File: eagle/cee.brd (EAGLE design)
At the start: 50 x 80 mm, 63 parts, among them IC1 IC1, J1 SOLDERJUMPERNC2

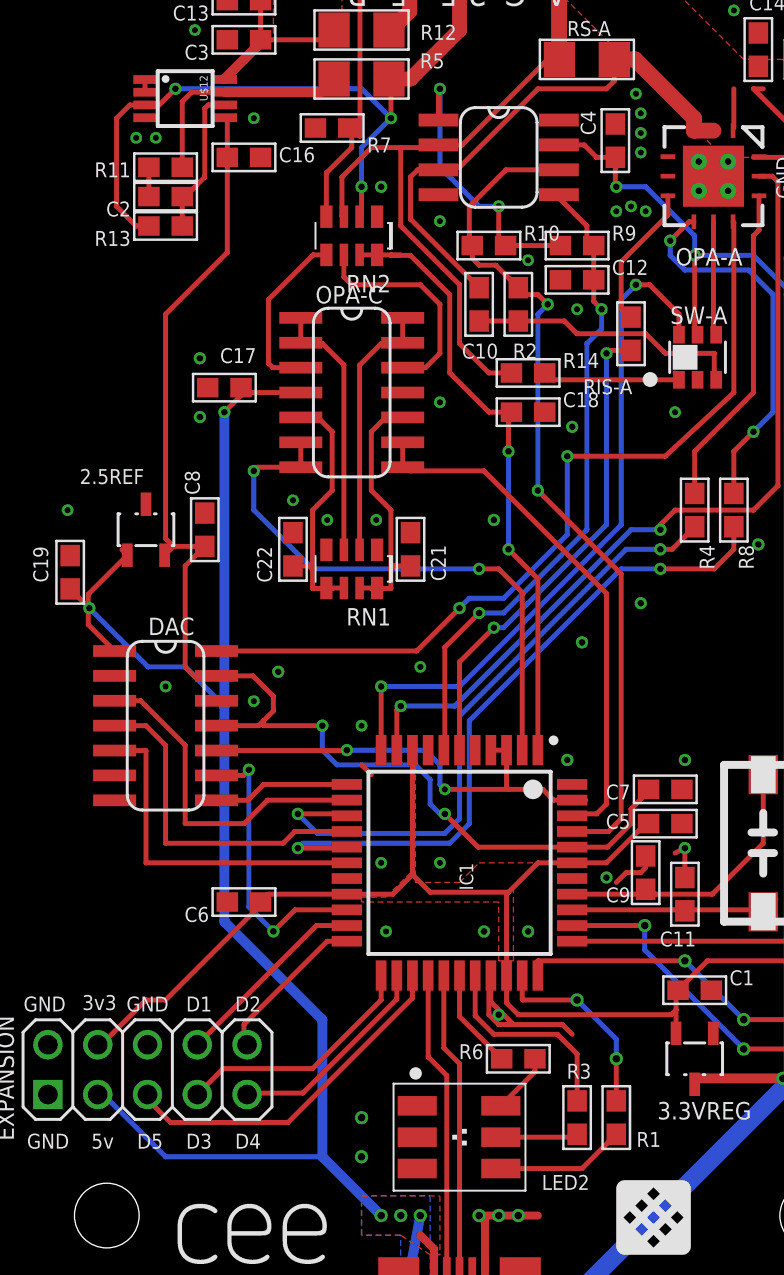
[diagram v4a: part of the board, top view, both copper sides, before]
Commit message: Connect CSA EN pin
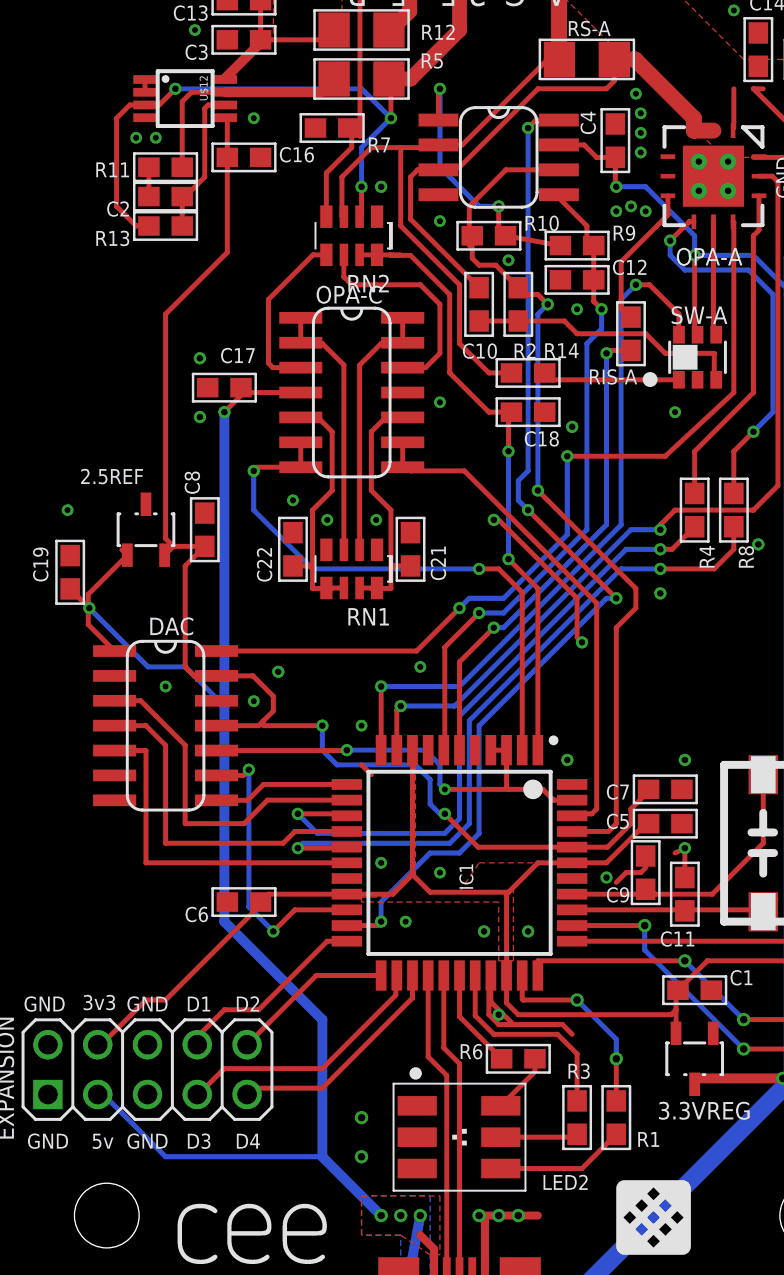
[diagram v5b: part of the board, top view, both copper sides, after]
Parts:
- moved R10 0.50 mm to (26.5, 57.0)
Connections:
- removed net EN-CSA: U$13.8
- removed net EXP5: EXPANSION.5, IC1.25
- new net CSA-EN: IC1.21, U$13.8
- net EXP1: now also IC1.22; no longer IC1.21
- net EXP2: now also IC1.23; no longer IC1.22
- net EXP3: now also IC1.24; no longer IC1.23
- net EXP4: now also IC1.25; no longer IC1.24
- net GND: now also EXPANSION.5
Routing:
- net CSA-EN: track 0.00 -> 52.5 mm, vias 0 -> 4
- net EXP5: track 18.1 -> 0.00 mm
- net GND: track 20.2 -> 27.9 mm
- net VS-A: track 44.0 -> 45.4 mm
- net ADC-A: track 27.2 -> 26.0 mm
- net EXP4: track 10.9 -> 11.7 mm
- net VOUT-B: track 23.3 -> 22.6 mm
- net EXP3: track 12.6 -> 13.3 mm
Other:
- board text removed: "D5"

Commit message: Rename VOUT-B -> ADCREF
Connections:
- net VOUT-B renamed ADCREF
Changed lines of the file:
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@@
 <wire x1="25.5" y1="38.5" x2="25" y2="38" width="0.254" layer="16"/>
 </signal>
-<signal name="VOUT-B">
+<signal name="ADCREF">
 <contactref element="DAC" pad="10"/>
 <contactref element="IC1" pad="4"/>

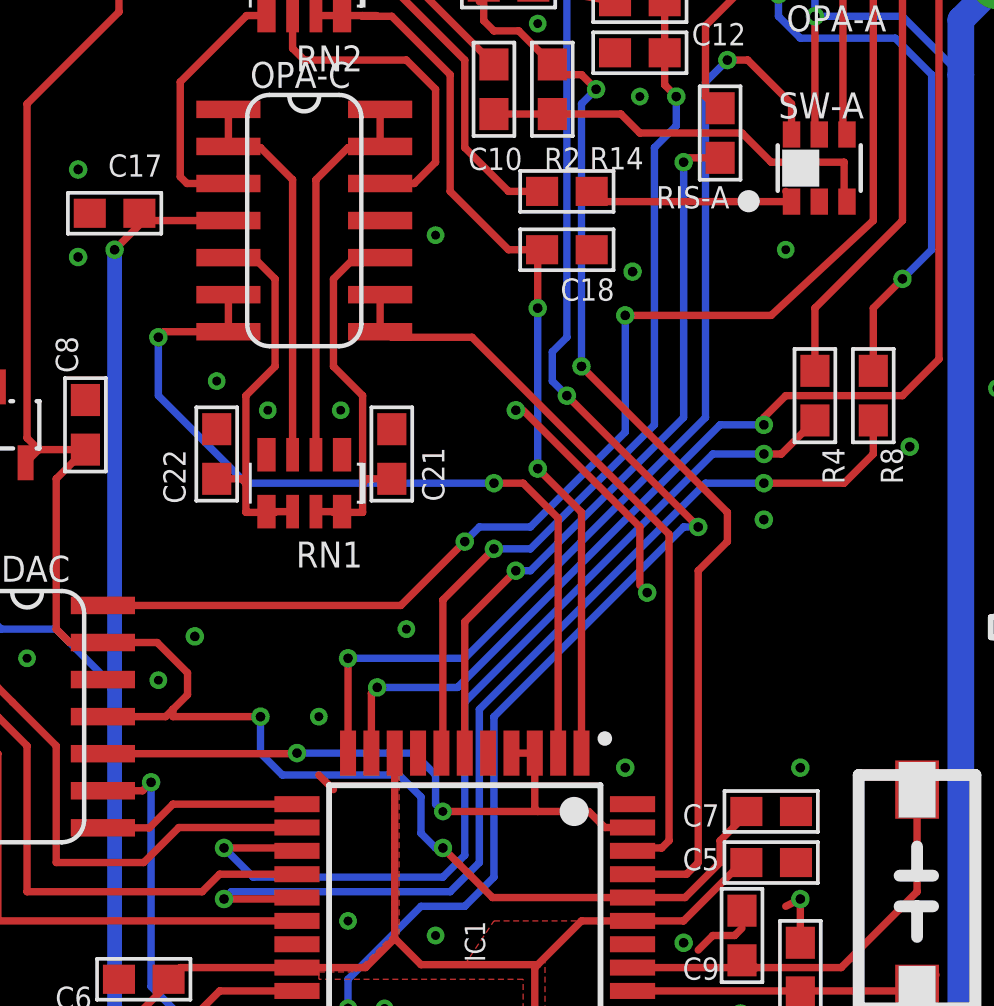
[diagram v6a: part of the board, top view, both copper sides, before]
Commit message: Clean up schematic
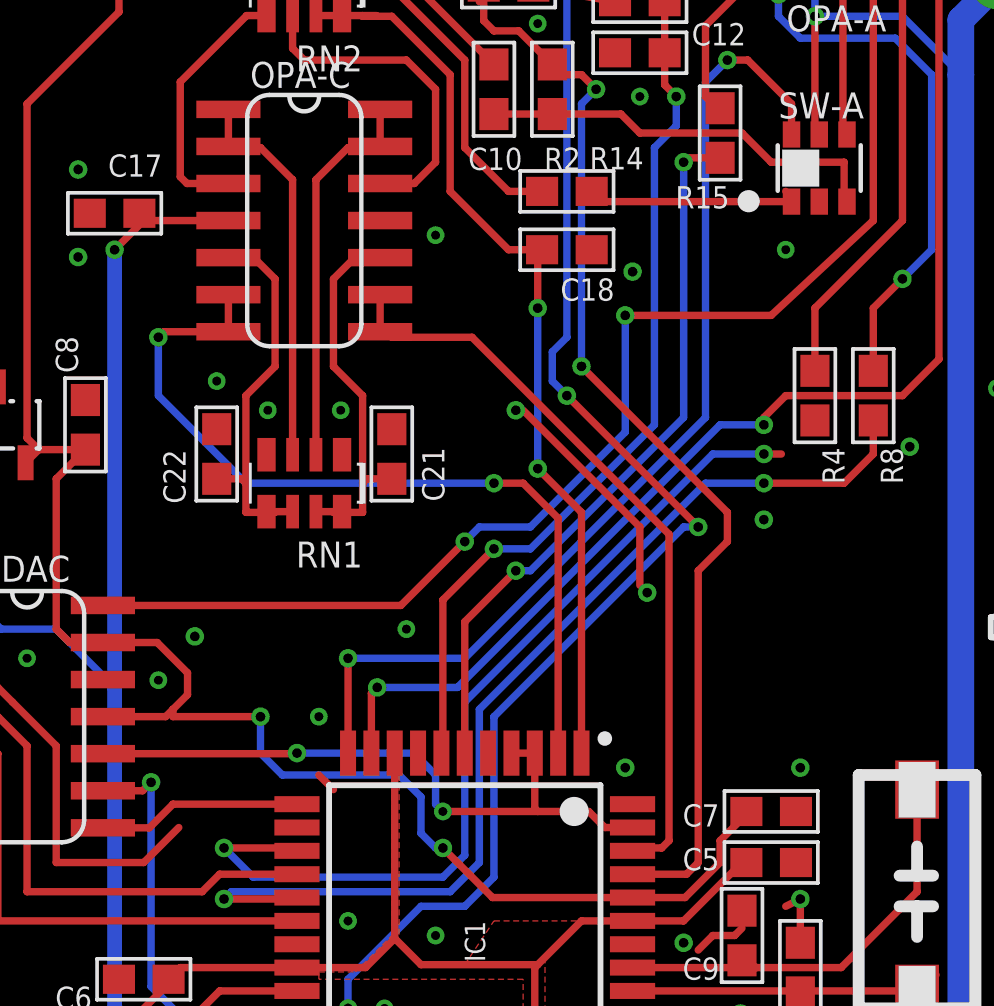
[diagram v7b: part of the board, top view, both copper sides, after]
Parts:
- renumbered RIS-A to R15
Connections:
- net CS: no longer IC1.13
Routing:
- net CS: track 17.3 -> 13.2 mm
- net TFLAG-P: track 33.1 -> 31.1 mm
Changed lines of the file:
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@@
 <attribute name="VALUE" x="10.905" y="45.429" size="1.27" layer="27" rot="R180"/>
 </element>
-<element name="RIS-A" library="nonolith" package="0603" value="5.6ko" x="33.75" y="52" smashed="yes" rot="R90">
+<element name="R15" library="nonolith" package="0603" value="5.6ko" x="33.75" y="52" smashed="yes" rot="R90">
 <attribute name="NAME" x="34.0708" y="50.1792" size="0.762" layer="25" font="vector" ratio="10" rot="R180"/>
 </element>
@@
 <signal name="CS">
 <contactref element="DAC" pad="3"/>
-<contactref element="IC1" pad="13"/>
-<wire x1="19.25" y1="28.2" x2="15.2" y2="28.2" width="0.254" layer="1"/>
 <wire x1="15.2" y1="28.2" x2="14" y2="27" width="0.254" layer="1"/>
 <wire x1="14" y1="27" x2="11" y2="27" width="0.254" layer="1"/>
@@
 </signal>
 <signal name="ISET-A">
-<contactref element="RIS-A" pad="2"/>
+<contactref element="R15" pad="2"/>
 <contactref element="OPA-A" pad="6"/>
 <wire x1="35.635" y1="58.0612" x2="35.635" y2="59.04" width="0.254" layer="1"/>
@@
 </signal>
 <signal name="ISET-DAC-A">
-<contactref element="RIS-A" pad="1"/>
+<contactref element="R15" pad="1"/>
 <contactref element="IC1" pad="6"/>
 <wire x1="33.75" y1="51.15" x2="32.65" y2="51.15" width="0.254" layer="1"/>
@@
 </signal>
 <signal name="TFLAG-P">
-<contactref element="R4" pad="2"/>
 <contactref element="IC1" pad="14"/>
-<wire x1="37" y1="42.15" x2="36.65" y2="42.15" width="0.254" layer="1"/>
 <via x="35.25" y="41" extent="1-16" drill="0.3302"/>
 <wire x1="25" y1="32.5" x2="25" y2="27.25" width="0.254" layer="16"/>
@@
 <wire x1="33.5" y1="41" x2="25" y2="32.5" width="0.254" layer="16"/>
 <wire x1="35.25" y1="41" x2="35.85" y2="41" width="0.254" layer="1"/>
-<wire x1="35.85" y1="41" x2="37" y2="42.15" width="0.254" layer="1"/>
+<contactref element="R4" pad="2"/>
+<wire x1="35.85" y1="41" x2="37" y2="42.15" width="0" layer="19" extent="1-1"/>
 </signal>
 <signal name="IFLAG-A">

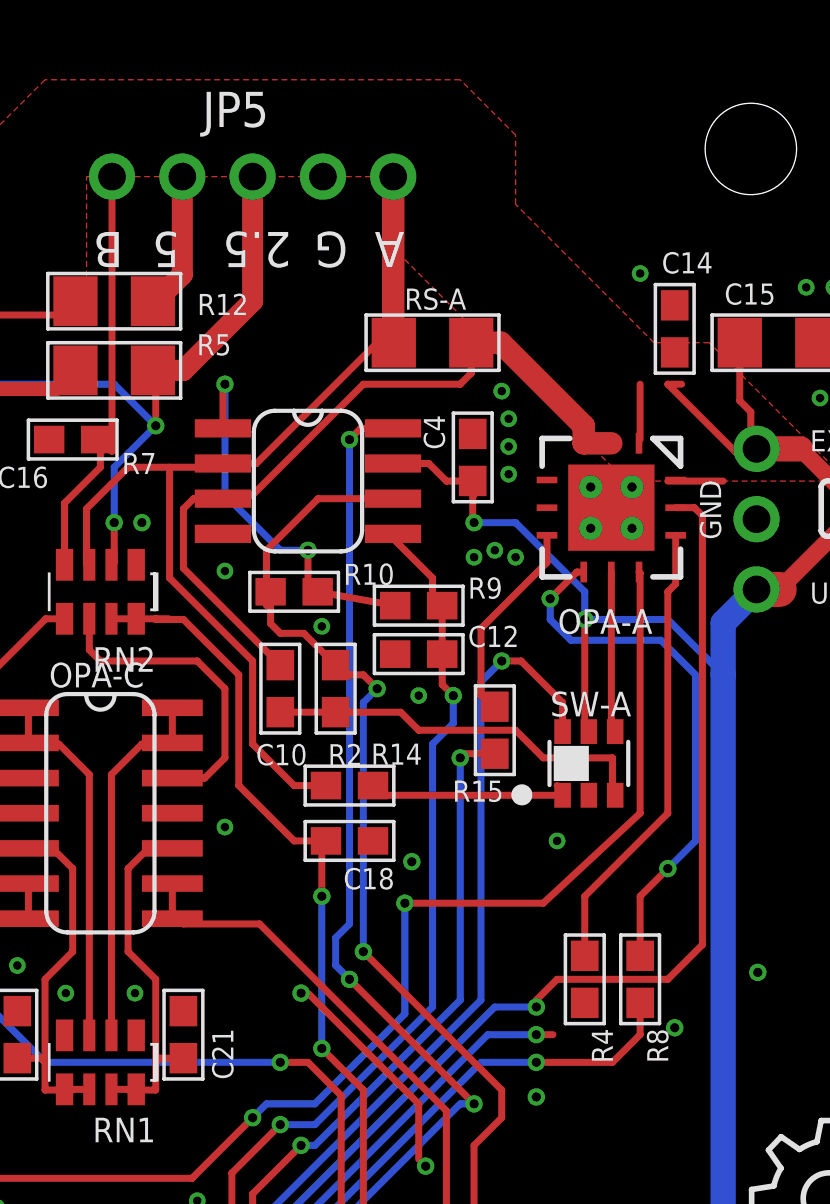
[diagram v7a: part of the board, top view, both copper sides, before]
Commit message: Reorganize schematic
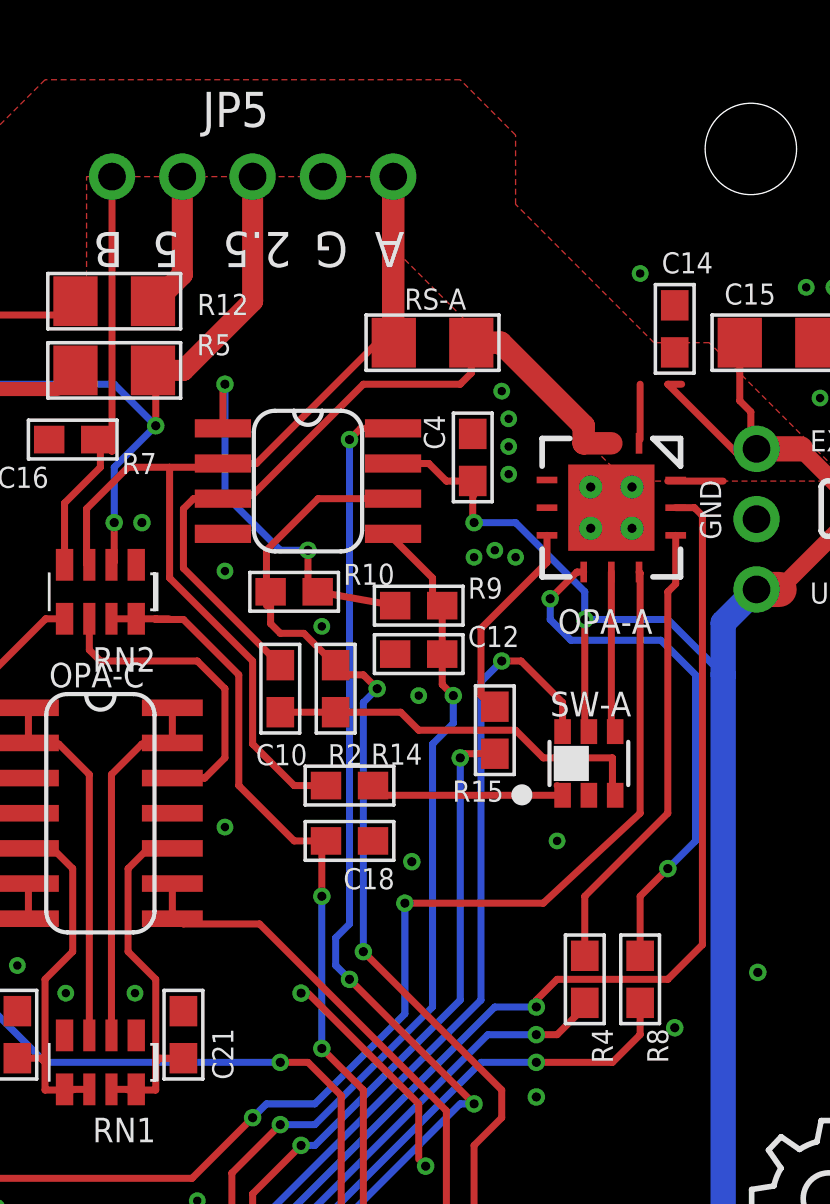
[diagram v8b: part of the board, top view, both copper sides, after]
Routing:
- net TFLAG-P: track 31.1 -> 32.9 mm
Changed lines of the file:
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@@
 <wire x1="9.1088" y1="35" x2="11" y2="35" width="0.254" layer="16"/>
 <wire x1="11" y1="35" x2="13" y2="33" width="0.254" layer="16"/>
-<contactref element="C17" pad="2"/>
-<wire x1="13.85" y1="49.25" x2="14" y2="49.1" width="0.254" layer="1"/>
 <wire x1="14" y1="49.1" x2="14" y2="49" width="0.254" layer="1"/>
 <wire x1="34.5" y1="59.5" x2="37" y2="57" width="0.254" layer="16"/>
@@
 <wire x1="32.75" y1="60.75" x2="32.75" y2="60.803" width="0.254" layer="1"/>
 <wire x1="32.75" y1="60.803" x2="32.952" y2="61.005" width="0.254" layer="1"/>
+<contactref element="C17" pad="2"/>
+<wire x1="13.85" y1="49.25" x2="14" y2="49.1" width="0.254" layer="1"/>
 </signal>
 <signal name="GND">
@@
 <via x="18.25" y="42.5" extent="1-16" drill="0.305"/>
 <via x="20.75" y="42.5" extent="1-16" drill="0.305"/>
-<contactref element="C17" pad="1"/>
 <via x="33.75" y="58.5" extent="1-16" drill="0.305"/>
 <via x="34.5" y="58.25" extent="1-16" drill="0.305"/>
@@
 <wire x1="31" y1="38.5" x2="27" y2="42.5" width="0.254" layer="1"/>
 <contactref element="EXPANSION" pad="5"/>
+<contactref element="C17" pad="1"/>
 </signal>
 <signal name="PDI-DATA">
@@
 <signal name="2.5VOUT">
 <contactref element="R5" pad="2"/>
-<contactref element="JP5" pad="3"/>
 <contactref element="R13" pad="2"/>
 <contactref element="U$12" pad="3"/>
-<wire x1="25" y1="72" x2="25" y2="67.5" width="0.762" layer="1"/>
 <wire x1="25" y1="67.5" x2="22.5" y2="65" width="0.762" layer="1"/>
 <wire x1="22.5" y1="65" x2="21.5" y2="65" width="0.762" layer="1"/>
@@
 <wire x1="21.5" y1="63" x2="20" y2="61.5" width="0.254" layer="16"/>
 <wire x1="20" y1="61.5" x2="20" y2="59.5" width="0.254" layer="16"/>
+<contactref element="JP5" pad="3"/>
+<wire x1="25" y1="67.5" x2="25" y2="72" width="0.762" layer="1"/>
 </signal>
 <signal name="2.5VFDBK">
@@
 <wire x1="35.25" y1="41" x2="33.5" y2="41" width="0.254" layer="16"/>
 <wire x1="33.5" y1="41" x2="25" y2="32.5" width="0.254" layer="16"/>
-<wire x1="35.25" y1="41" x2="35.85" y2="41" width="0.254" layer="1"/>
+<wire x1="35.25" y1="41" x2="36" y2="41" width="0.254" layer="1"/>
 <contactref element="R4" pad="2"/>
-<wire x1="35.85" y1="41" x2="37" y2="42.15" width="0" layer="19" extent="1-1"/>
+<wire x1="36" y1="41" x2="37" y2="42" width="0.254" layer="1"/>
+<wire x1="37" y1="42" x2="37" y2="42.15" width="0.254" layer="1"/>
 </signal>
 <signal name="IFLAG-A">
